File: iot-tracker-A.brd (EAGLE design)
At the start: 23.5 x 20 mm, 22 parts, among them U1 ESP-WROOM-02, U2 TPL5111DDCR, U3 MCP1640T-I_CHY

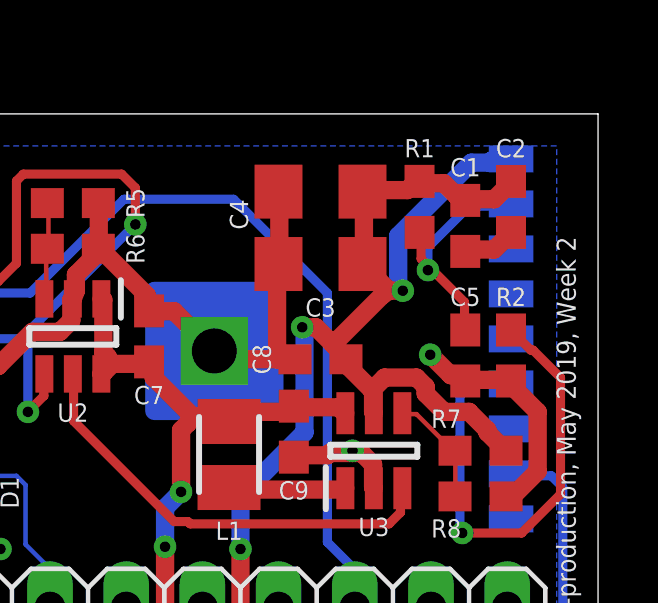
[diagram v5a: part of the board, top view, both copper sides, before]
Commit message: Routed C1 to ground plane
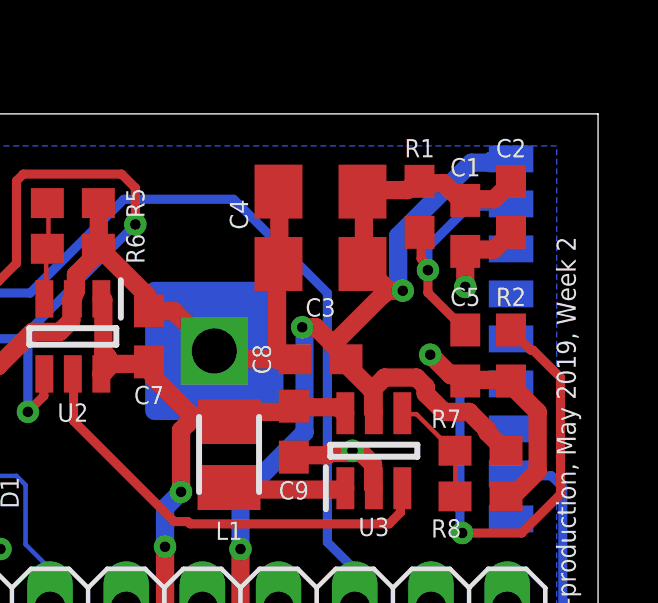
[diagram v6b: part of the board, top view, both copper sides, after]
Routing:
- net GND: track 40.4 -> 41.6 mm, vias 2 -> 3
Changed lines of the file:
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@@
 <wire x1="19.7358" y1="15.4686" x2="19.685" y2="15.406" width="0.6096" layer="1"/>
 <wire x1="21.1836" y1="16.002" x2="21.209" y2="16.041" width="0.6096" layer="1"/>
-<wire x1="18.5166" y1="11.9634" x2="19.685" y2="15.406" width="0" layer="19" extent="1-1"/>
+<wire x1="19.685" y1="15.406" x2="19.685" y2="14.224" width="0.6096" layer="1"/>
+<via x="19.685" y="14.224" extent="1-16" drill="0.35"/>
 </signal>
 <signal name="DONE" class="2">
@@
 <contactref element="R1" pad="2"/>
 <contactref element="C5" pad="2"/>
-<wire x1="19.6596" y1="13.716" x2="19.6596" y2="12.8016" width="0.3048" layer="1"/>
 <wire x1="18.2118" y1="15.1638" x2="18.5166" y2="14.859" width="0.3048" layer="1"/>
-<wire x1="18.5166" y1="14.859" x2="19.6596" y2="13.716" width="0.3048" layer="1"/>
 <wire x1="18.2118" y1="16.002" x2="18.2118" y2="15.1638" width="0.3048" layer="1"/>
-<wire x1="19.6596" y1="12.8016" x2="19.685" y2="12.788" width="0.3048" layer="1"/>
 <wire x1="18.2118" y1="16.002" x2="18.161" y2="16.041" width="0.3048" layer="1"/>
 <wire x1="19.812" y1="16.9164" x2="21.1836" y2="16.9164" width="0.3048" layer="16"/>
@@
 <wire x1="18.4404" y1="14.7828" x2="18.5166" y2="14.859" width="0.3048" layer="1"/>
 <via x="18.4404" y="14.7828" extent="1-16" drill="0.35"/>
+<wire x1="19.685" y1="12.788" x2="18.4404" y2="14.0326" width="0.3048" layer="1"/>
+<wire x1="18.4404" y1="14.0326" x2="18.4404" y2="14.7828" width="0.3048" layer="1"/>
 </signal>
 <signal name="DELAY">

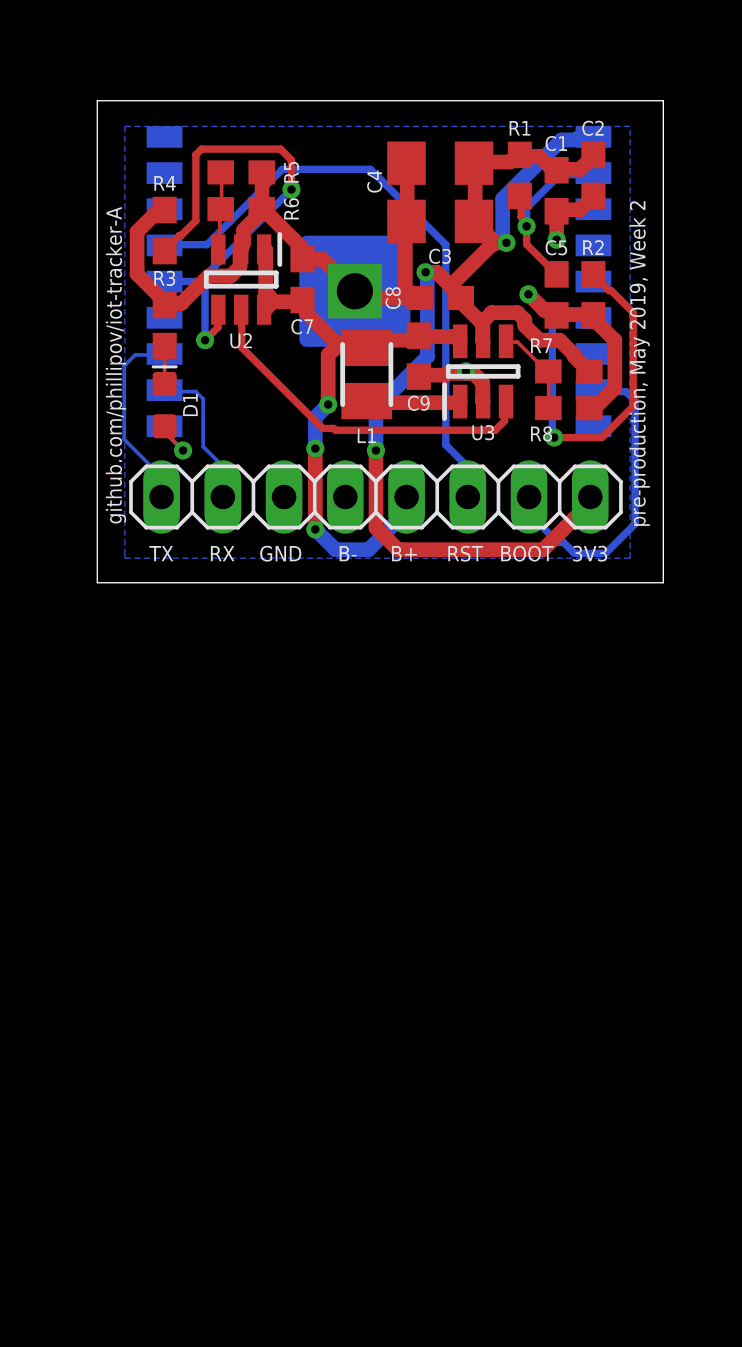
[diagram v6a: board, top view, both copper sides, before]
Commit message: Started phasing out the MCP1640 boost converter
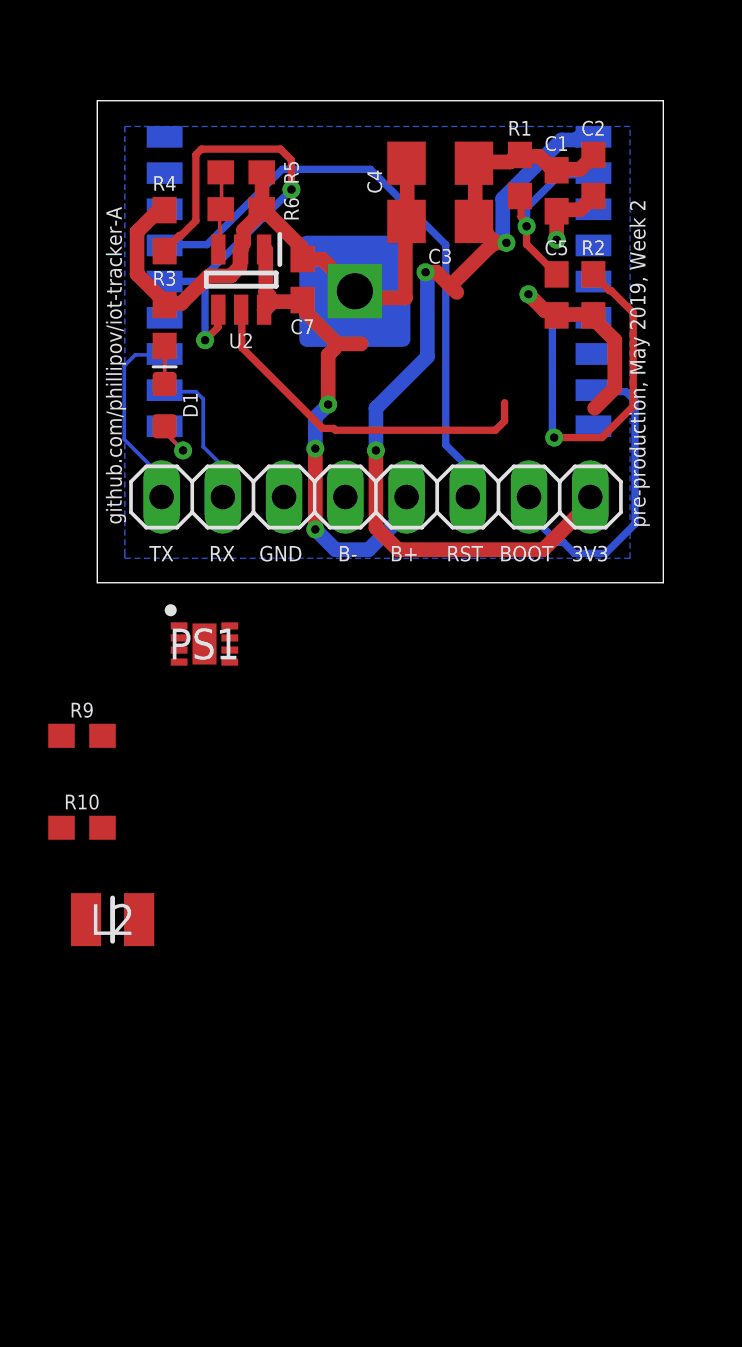
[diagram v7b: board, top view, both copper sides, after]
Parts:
- removed C8, C9: 10uF, SparkFun-Capacitors:0603
- removed L1: MAMK2520T4R7M, MAMK2520T4R7M:INDM2520X120N
- removed R7: 976k, SparkFun-Resistors:0603
- removed R8: 562k, SparkFun-Resistors:0603
- removed U3: MCP1640T-I_CHY, MCP1640T-I_CHY:SOT95P270X145-6N
- added L2: 0.47uH, IOT-Tracker-A:INDC2520X120N
- added PS1: TPS61021ADSGR, IOT-Tracker-A:SON50P200X200X80-9N
- added R10: 100k, SparkFun-Resistors:0603
- added R9: 316k, SparkFun-Resistors:0603
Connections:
- removed net SW: L1.1, U3.1
- removed net VFB: R7.2, R8.1, U3.4
- new net N$1: PS1.2, R10.1, R9.2
- new net N$3: L2.1, PS1.6, PS1.7
- net 3.3V: now also PS1.3, PS1.4, R9.1; no longer C8.2, R7.1, U3.5
- net DRVN: now also PS1.5; no longer U3.3
- net GND: now also PS1.1, PS1.9, R10.2; no longer C8.1, C9.1, R8.2, U3.2
- net V_BATT: now also L2.2, PS1.8; no longer C9.2, L1.2, U3.6
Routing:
- net 3.3V: track 50.8 -> 42.5 mm
- net GND: track 41.6 -> 37.0 mm, vias 3 -> 2
- net V_BATT: track 25.7 -> 21.3 mm
- net SW: track 3.96 -> 0.00 mm
- net VFB: track 3.83 -> 0.00 mm

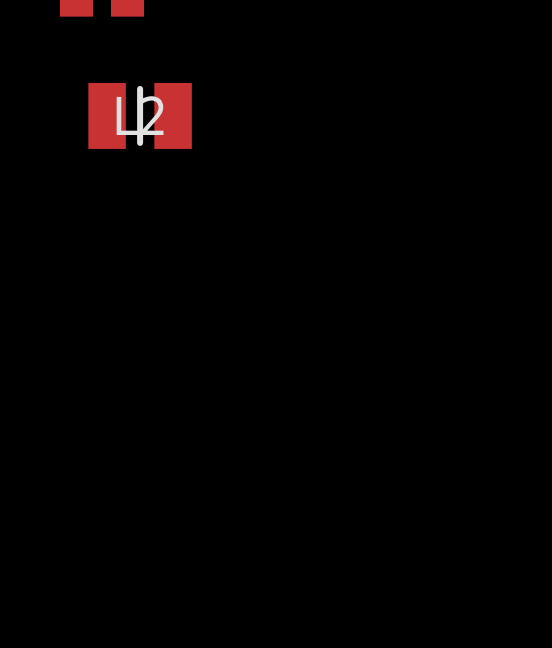
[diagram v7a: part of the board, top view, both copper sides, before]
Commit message: Integrated the TPS61021A into the schematic
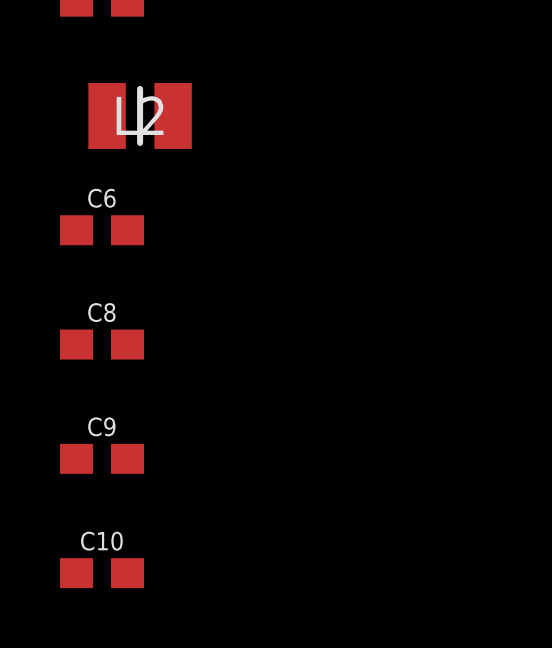
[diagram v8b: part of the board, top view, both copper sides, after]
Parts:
- added C10, C9: 10uF, SparkFun-Capacitors:0603
- added C6: 0.1uF, SparkFun-Capacitors:0603
- added C8: 100pF, SparkFun-Capacitors:0603
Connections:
- net N$3 renamed SW
- net 3.3V: now also C10.1, C8.2, C9.1
- net GND: now also C10.2, C6.1, C9.2
- net N$1: now also C8.1
- net V_BATT: now also C6.2
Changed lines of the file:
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@@
 <attribute name="VALUE" x="1.27" y="-13.97" size="1.27" layer="27" align="center"/>
+</element>
+<element name="C6" library="SparkFun-Capacitors" package="0603" value="0.1uF" x="0" y="-17.78" smashed="yes">
+<attribute name="NAME" x="0" y="-17.018" size="0.6096" layer="25" font="vector" ratio="20" align="bottom-center"/>
+<attribute name="PROD_ID" value="CAP-00810" x="0" y="-17.78" size="1.778" layer="27" display="off"/>
+<attribute name="VALUE" x="0" y="-18.542" size="0.6096" layer="27" font="vector" ratio="20" align="top-center"/>
+</element>
+<element name="C8" library="SparkFun-Capacitors" package="0603" value="100pF" x="0" y="-21.59" smashed="yes">
+<attribute name="NAME" x="0" y="-20.828" size="0.6096" layer="25" font="vector" ratio="20" align="bottom-center"/>
+<attribute name="PROD_ID" value="CAP-07883" x="0" y="-21.59" size="1.778" layer="27" display="off"/>
+<attribute name="VALUE" x="0" y="-22.352" size="0.6096" layer="27" font="vector" ratio="20" align="top-center"/>
+</element>
+<element name="C9" library="SparkFun-Capacitors" library_urn="urn:adsk.eagle:library:510" package="0603" package3d_urn="urn:adsk.eagle:package:37414/1" value="10uF" x="0" y="-25.4" smashed="yes">
+<attribute name="NAME" x="0" y="-24.638" size="0.6096" layer="25" font="vector" ratio="20" align="bottom-center"/>
+<attribute name="PROD_ID" value="CAP-11015" x="0" y="-25.4" size="1.778" layer="27" display="off"/>
+<attribute name="VALUE" x="0" y="-26.162" size="0.6096" layer="27" font="vector" ratio="20" align="top-center"/>
+</element>
+<element name="C10" library="SparkFun-Capacitors" library_urn="urn:adsk.eagle:library:510" package="0603" package3d_urn="urn:adsk.eagle:package:37414/1" value="10uF" x="0" y="-29.21" smashed="yes">
+<attribute name="NAME" x="0" y="-28.448" size="0.6096" layer="25" font="vector" ratio="20" align="bottom-center"/>
+<attribute name="PROD_ID" value="CAP-11015" x="0" y="-29.21" size="1.778" layer="27" display="off"/>
+<attribute name="VALUE" x="0" y="-29.972" size="0.6096" layer="27" font="vector" ratio="20" align="top-center"/>
 </element>
 </elements>
@@
 <contactref element="R10" pad="2"/>
 <contactref element="PS1" pad="1"/>
+<contactref element="C6" pad="1"/>
+<contactref element="C9" pad="2"/>
+<contactref element="C10" pad="2"/>
 <wire x1="18.5166" y1="11.9634" x2="19.685" y2="14.224" width="0" layer="19" extent="1-1"/>
 <wire x1="21.2115" y1="6.489" x2="21.2598" y2="7.239" width="0" layer="19" extent="1-16"/>
@@
 <wire x1="5.08" y1="-2.54" x2="4.03" y2="-1.79" width="0" layer="19" extent="1-1"/>
 <wire x1="0.85" y1="-10.16" x2="5.08" y2="-2.54" width="0" layer="19" extent="1-1"/>
+<wire x1="-0.85" y1="-17.78" x2="0.85" y2="-10.16" width="0" layer="19" extent="1-1"/>
+<wire x1="0.85" y1="-25.4" x2="-0.85" y2="-17.78" width="0" layer="19" extent="1-1"/>
+<wire x1="0.85" y1="-29.21" x2="0.85" y2="-25.4" width="0" layer="19" extent="1-1"/>
 </signal>
 <signal name="DONE" class="2">
@@
 <contactref element="R9" pad="1"/>
 <contactref element="PS1" pad="4"/>
-<wire x1="4.03" y1="-2.79" x2="12.192" y2="2.286" width="0" layer="19" extent="1-1"/>
-<wire x1="4.03" y1="-3.29" x2="4.03" y2="-2.79" width="0" layer="19" extent="1-1"/>
-<wire x1="-0.85" y1="-6.35" x2="4.03" y2="-3.29" width="0" layer="19" extent="1-1"/>
+<contactref element="C8" pad="2"/>
+<contactref element="C9" pad="1"/>
+<contactref element="C10" pad="1"/>
+<wire x1="-0.85" y1="-25.4" x2="-0.85" y2="-29.21" width="0" layer="19" extent="1-1"/>
+<wire x1="0.85" y1="-21.59" x2="-0.85" y2="-25.4" width="0" layer="19" extent="1-1"/>
+<wire x1="-0.85" y1="-6.35" x2="0.85" y2="-21.59" width="0" layer="19" extent="1-1"/>
+<wire x1="4.03" y1="-3.29" x2="-0.85" y2="-6.35" width="0" layer="19" extent="1-1"/>
+<wire x1="4.03" y1="-2.79" x2="4.03" y2="-3.29" width="0" layer="19" extent="1-1"/>
+<wire x1="12.192" y1="2.286" x2="4.03" y2="-2.79" width="0" layer="19" extent="1-1"/>
 </signal>
 <signal name="V_BATT" class="1">
@@
 <contactref element="PS1" pad="8"/>
 <contactref element="L2" pad="2"/>
+<contactref element="C6" pad="2"/>
+<wire x1="2.37" y1="-13.97" x2="0.85" y2="-17.78" width="0" layer="19" extent="1-1"/>
 <wire x1="6.13" y1="-1.79" x2="2.37" y2="-13.97" width="0" layer="19" extent="1-1"/>
 <wire x1="9.6774" y1="2.2098" x2="6.13" y2="-1.79" width="0" layer="19" extent="1-16"/>
@@
 <contactref element="R10" pad="1"/>
 <contactref element="R9" pad="2"/>
+<contactref element="C8" pad="1"/>
+<wire x1="-0.85" y1="-10.16" x2="-0.85" y2="-21.59" width="0" layer="19" extent="1-1"/>
 <wire x1="0.85" y1="-6.35" x2="-0.85" y2="-10.16" width="0" layer="19" extent="1-1"/>
 <wire x1="4.03" y1="-2.29" x2="0.85" y2="-6.35" width="0" layer="19" extent="1-1"/>
 </signal>
-<signal name="N$3">
+<signal name="SW">
 <contactref element="PS1" pad="6"/>
 <contactref element="PS1" pad="7"/>
